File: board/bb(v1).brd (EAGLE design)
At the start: 20.3 x 57.2 mm, 1 part

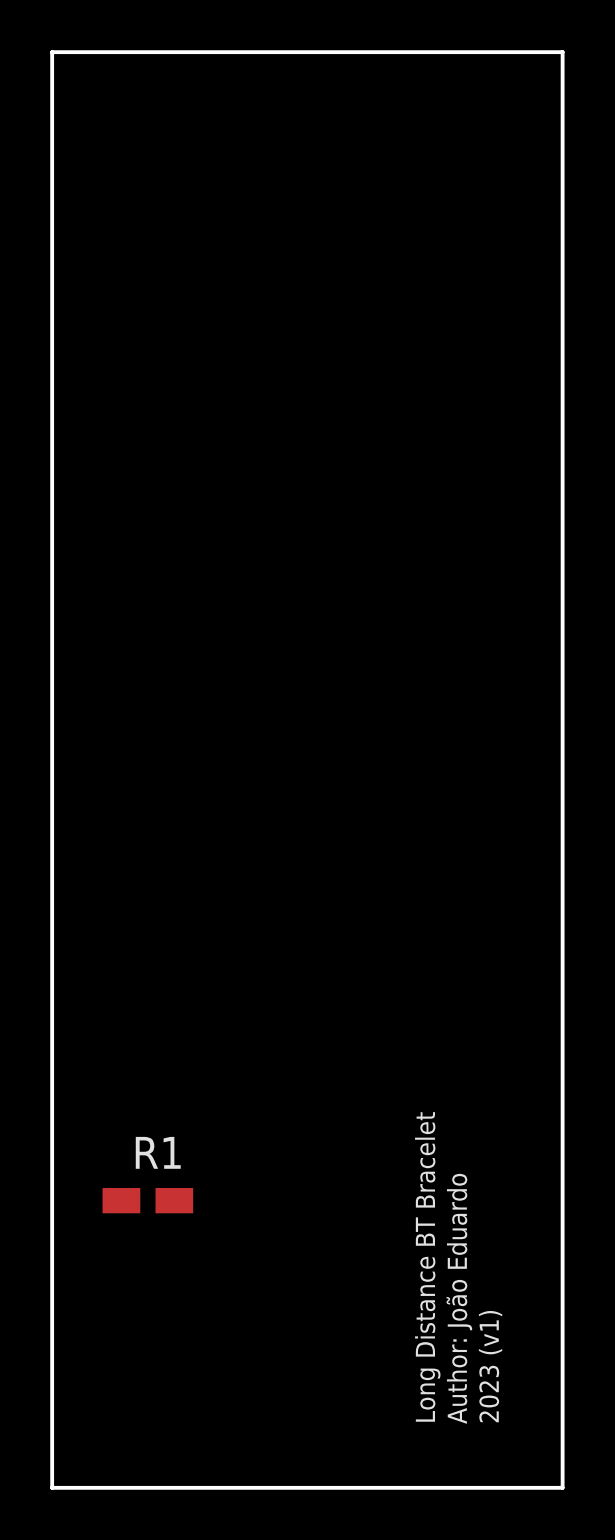
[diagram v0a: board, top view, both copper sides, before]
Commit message: Adição do módulo bluetooth na placa
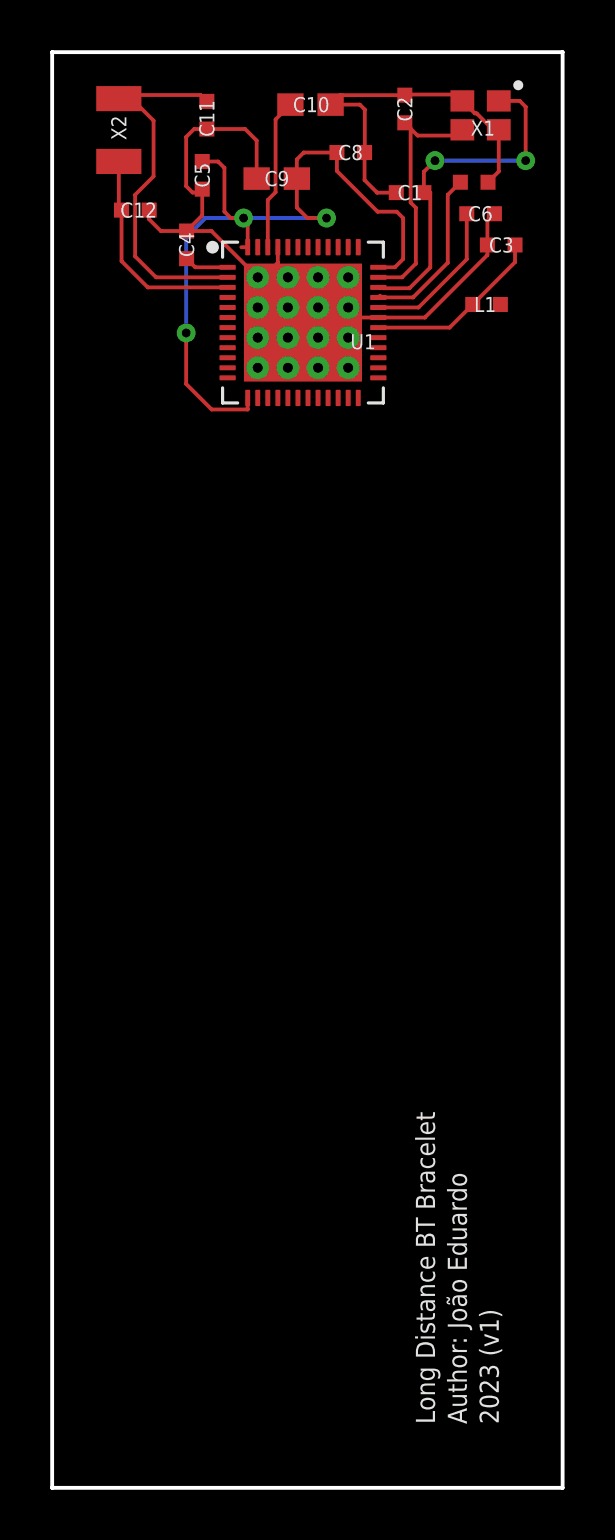
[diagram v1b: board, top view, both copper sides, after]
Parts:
- removed R1: (no value), rcl:R0805W
- added C1, C11, C12, C2: 12pF, Nordic_nRF:RESC0402_N
- added C10: 1.0µF, Nordic_nRF:RESC0603_N
- added C3: 0.8pF, Nordic_nRF:RESC0402_N
- added C4, C5, C8: 100nF, Nordic_nRF:RESC0402_N
- added C6: N.M., Nordic_nRF:RESC0402_N
- added C7: 100pF, Nordic_nRF:RESC0402_N
- added C9: 4.7µF, Nordic_nRF:RESC0603_N
- added L1: 3.9nH, Nordic_nRF:RESC0402_N
- added U1: NRF52832, Nordic_nRF:QFN40P600X600X90-48_N
- added X1: 32MHz, Nordic_nRF:BT-XTAL_2016_N
- added X2: 32.768kHz, Nordic_nRF:XTAL_3215_N
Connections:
- new net ANT: C3.1, L1.1, U1.30
- new net DEC1: C4.1, U1.1
- new net DEC2: C6.1, U1.32
- new net DEC3: C7.1, U1.33
- new net DEC4: C10.1, U1.46
- new net GND: C1.2, C10.2, C11.1, C12.1, C2.2, C3.2, C4.2, C5.2, C6.2, C7.2, C8.2, C9.2, U1.31, U1.45, U1.PAD, U1.PAD@VIA01, U1.PAD@VIA02, U1.PAD@VIA03, U1.PAD@VIA04, U1.PAD@VIA05, U1.PAD@VIA06, U1.PAD@VIA07, U1.PAD@VIA08, U1.PAD@VIA09, U1.PAD@VIA10, U1.PAD@VIA11, U1.PAD@VIA12, U1.PAD@VIA13, U1.PAD@VIA14, U1.PAD@VIA15, U1.PAD@VIA16, X1.2, X1.4
- new net N$3: C2.1, U1.35, X1.3
- new net P0.00/XL1: C11.2, U1.2, X2.1
- new net P0.01/XL2: C12.2, U1.3, X2.2
- new net P0.02: U1.4
- new net P0.03: U1.5
- new net P0.04: U1.6
- new net P0.05: U1.7
- new net P0.06: U1.8
- new net P0.07: U1.9
- new net P0.08: U1.10
- new net P0.09: U1.11
- new net P0.10: U1.12
- new net P0.11: U1.14
- new net P0.12: U1.15
- new net P0.13: U1.16
- new net P0.14: U1.17
- new net P0.15: U1.18
- new net P0.16: U1.19
- new net P0.17: U1.20
- new net P0.18/SWO: U1.21
- new net P0.19: U1.22
- new net P0.20: U1.23
- new net P0.21/RESET: U1.24
- new net P0.22: U1.27
- new net P0.23: U1.28
- new net P0.24: U1.29
- new net P0.25: U1.37
- new net P0.26: U1.38
- new net P0.27: U1.39
- new net P0.28: U1.40
- new net P0.29: U1.41
- new net P0.30: U1.42
- new net P0.31: U1.43
- new net RF: L1.2
- new net SWDCLK: U1.25
- new net SWDIO: U1.26
- new net VDD_P3V3: C5.1, C8.1, C9.1, U1.13, U1.36, U1.48
- new net X1: C1.1, U1.34, X1.1
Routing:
- net GND: track 0.00 -> 44.1 mm
- net VDD_P3V3: track 0.00 -> 32.3 mm, vias 0 -> 3
- net P0.00/XL1: track 0.00 -> 15.1 mm
- net X1: track 0.00 -> 14.0 mm, vias 0 -> 2
- net N$3: track 0.00 -> 10.1 mm
- net P0.01/XL2: track 0.00 -> 8.67 mm
- net ANT: track 0.00 -> 7.20 mm
- net DEC3: track 0.00 -> 6.85 mm
- net DEC2: track 0.00 -> 6.13 mm
- net DEC4: track 0.00 -> 6.05 mm
- net DEC1: track 0.00 -> 1.77 mm
